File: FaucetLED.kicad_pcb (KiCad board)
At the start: 2 copper layers, 29.2 x 33.3 mm, 25 parts, among them P1 CONN_01X13, P2 CONN_01X02, U1 MAX4256

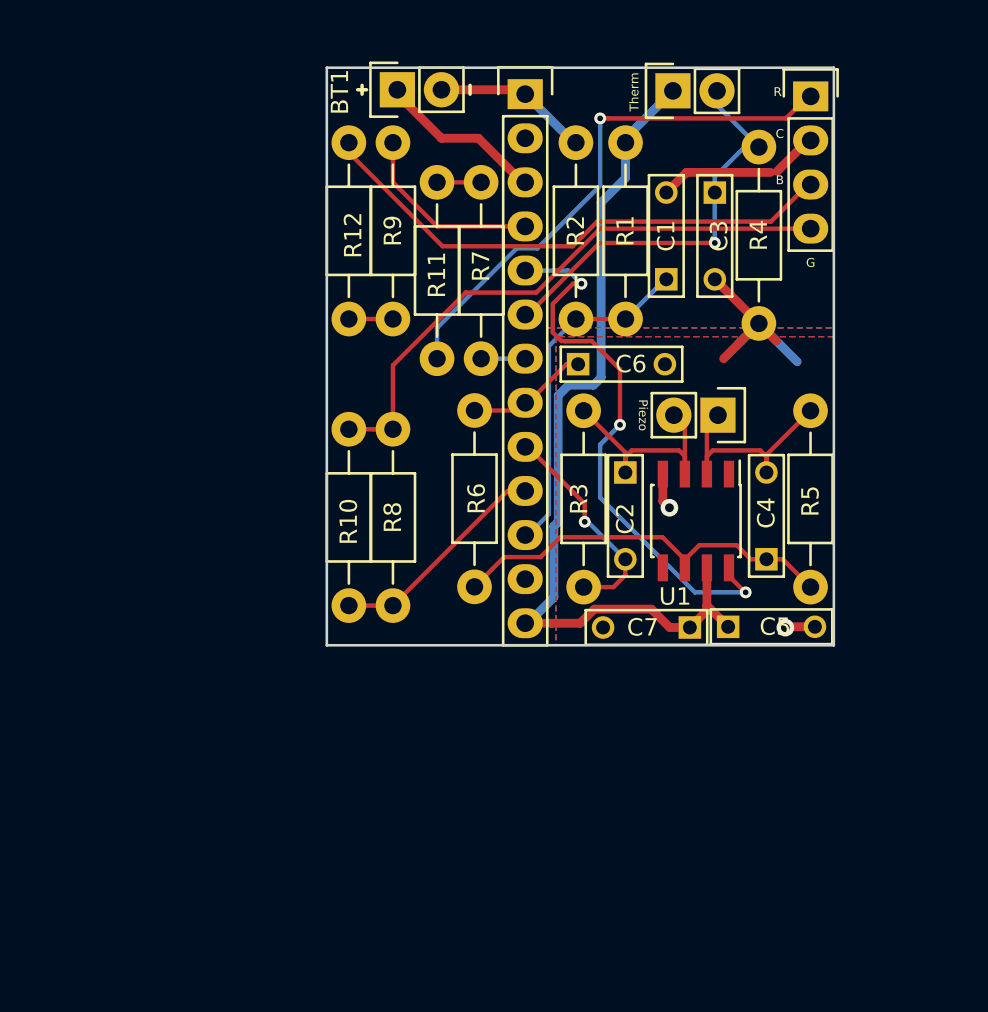
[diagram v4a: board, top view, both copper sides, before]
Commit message: WIP version 2 with STM32L0.
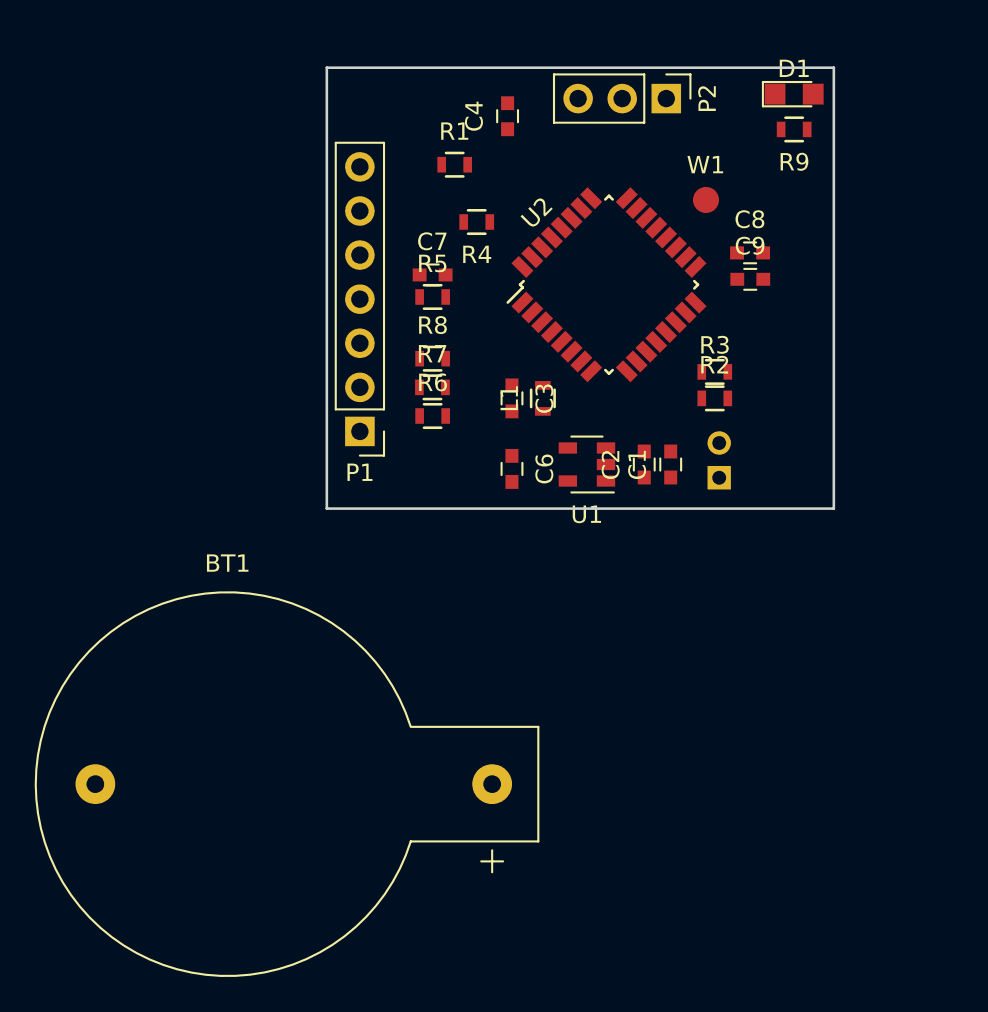
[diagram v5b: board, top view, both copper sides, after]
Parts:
- removed C5: 0.1u, Capacitors_ThroughHole:C_Rect_L7_W2_P5
- removed R10: 68R, Resistors_ThroughHole:Resistor_Horizontal_RM10mm
- removed R11, R12: 10R, Resistors_ThroughHole:Resistor_Horizontal_RM10mm
- removed TH1: THERMISTOR, Pin_Headers:Pin_Header_Straight_1x02
- added BT2: LiIon, Pin_Headers:Pin_Header_Angled_1x02_Pitch2.00mm, B.Cu at (124.2, 99.8)
- added C8: 0.1u, Capacitors_SMD:C_0603, F.Cu at (126.0, 86.9)
- added C9: 1u, Capacitors_SMD:C_0603, F.Cu at (126.0, 88.4)
- added L1: Bead, Resistors_SMD:R_0603, F.Cu at (114.0, 95.2)
- added U2: STM32L052KxTx, Housings_QFP:LQFP-32_7x7mm_Pitch0.8mm, F.Cu at (117.9, 88.7)
- added W1: TEST_1P, Measurement_Points:Measurement_Point_Round-SMD-Pad_Small, F.Cu at (123.4, 83.8)
- BT1: value Battery -> CR2016x2; footprint Pin_Headers:Pin_Header_Straight_1x02 -> Connect:CR2032H
- C1: value 10n -> 0.1u; footprint Capacitors_ThroughHole:C_Rect_L7_W2_P5 -> Capacitors_SMD:C_0603
- C2: value 10p -> 1u; footprint Capacitors_ThroughHole:C_Rect_L7_W2_P5 -> Capacitors_SMD:C_0603
- C3, C7: value 1u -> 0.1u; footprint Capacitors_ThroughHole:C_Rect_L7_W2_P5 -> Capacitors_SMD:C_0603
- C4: value 10p -> 0.47u; footprint Capacitors_ThroughHole:C_Rect_L7_W2_P5 -> Capacitors_SMD:C_0603
- C6: value 0.1u -> 1u; footprint Capacitors_ThroughHole:C_Rect_L7_W2_P5 -> Capacitors_SMD:C_0603
- D1: value LED_RCBG -> LED; footprint Pin_Headers:Pin_Header_Straight_1x04 -> LEDs:LED_0805
- P1: value CONN_01X13 -> CONN_01X07; footprint Socket_Strips:Socket_Strip_Straight_1x13 -> Pin_Headers:Pin_Header_Straight_1x07_Pitch2.54mm
- P2: value CONN_01X02 -> CONN_01X03; footprint Pin_Headers:Pin_Header_Straight_1x02 -> Pin_Headers:Pin_Header_Straight_1x03_Pitch2.54mm
- R1: value 1M -> 100R; footprint Resistors_ThroughHole:Resistor_Horizontal_RM10mm -> Resistors_SMD:R_0603
- R2, R4: footprint Resistors_ThroughHole:Resistor_Horizontal_RM10mm -> Resistors_SMD:R_0603
- R3: value 100M -> 1M; footprint Resistors_ThroughHole:Resistor_Horizontal_RM10mm -> Resistors_SMD:R_0603
- R5: value 100M -> 10k; footprint Resistors_ThroughHole:Resistor_Horizontal_RM10mm -> Resistors_SMD:R_0603
- R6: value 680R -> 78R; footprint Resistors_ThroughHole:Resistor_Horizontal_RM10mm -> Resistors_SMD:R_0603
- R7: value 68R -> 12R; footprint Resistors_ThroughHole:Resistor_Horizontal_RM10mm -> Resistors_SMD:R_0603
- R8: value 15R -> 25R; footprint Resistors_ThroughHole:Resistor_Horizontal_RM10mm -> Resistors_SMD:R_0603
- R9: value 15R -> 1k; footprint Resistors_ThroughHole:Resistor_Horizontal_RM10mm -> Resistors_SMD:R_0603
- U1: value MAX4256 -> TLV70033DDC; footprint Housings_SOIC:SOIC-8_3.9x4.9mm_Pitch1.27mm -> TO_SOT_Packages_SMD:SOT-23-5
- moved BT1 40.4 mm to (111.1, 117.5), turned to 0 degrees
- moved C4 29.6 mm to (112.0, 79.0)
- moved R5 27.4 mm to (107.7, 89.4), turned to 0 degrees
- moved R9 25.6 mm to (128.5, 79.8), turned to 180 degrees
- moved C7 25.1 mm to (107.7, 88.1), turned to 0 degrees
- moved P1 21.6 mm to (103.5, 97.2), turned to 180 degrees
- moved P2 18.5 mm to (121.2, 78.0)
- moved R4 16.8 mm to (110.2, 85.1), turned to 180 degrees
- moved C3 16.6 mm to (112.3, 95.2)
- moved R7 12.1 mm to (107.7, 94.6), turned to 0 degrees
- moved C1 10.7 mm to (121.4, 99.1)
- moved R1 9.92 mm to (109.0, 81.8), turned to 0 degrees
- moved R2 9.22 mm to (124.0, 95.2), turned to 0 degrees
- moved R3 7.88 mm to (124.0, 93.7), turned to 0 degrees
- moved C6 7.13 mm to (112.3, 99.3), turned to 270 degrees
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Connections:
- C1 pad 1: /VCC_2 -> +BATT
- C2 pad 1: /PIEZO_2 -> +BATT
- C2 pad 2: /VCC_2_BUF -> GND
- C3 pad 1: /THERM_2 -> /RESET
- C4 pad 1: Net-(C4-Pad1) -> /TSC_SAMPLING
- C4 pad 2: /PIEZO_1 -> GND
- C6 pad 1: /PIEZO_AMP -> +3V3
- C7 pad 1: +3V3 -> /THERM_SENSE
- D1 pad 1: Net-(D1-Pad1) -> GND
- D1 pad 2: GND -> Net-(D1-Pad2)
- P1 pad 1: GND -> /LED_R_OUT
- P1 pad 2: (no net) -> /LED_G_OUT
- P1 pad 3: +BATT -> /LED_B_OUT
- P1 pad 4: /LED_B -> GND
- P1 pad 5: /AMP_SHDN -> /THERM_SW
- P1 pad 6: /THERM_2 -> /THERM_SENSE
- P1 pad 7: /LED_R -> /TSC_IN
- P2 pad 1: /PIEZO_1 -> /SWDIO
- P2 pad 2: /PIEZO_2 -> /SWCLK
- R1 pad 1: +3V3 -> /TSC_IN
- R1 pad 2: /VCC_2 -> Net-(R1-Pad2)
- R2 pad 1: /VCC_2 -> +BATT
- R2 pad 2: GND -> /BATT_2
- R3 pad 1: /PIEZO_2 -> /BATT_2
- R3 pad 2: /VCC_2_BUF -> GND
- R4 pad 1: /THERM_2 -> Net-(R4-Pad1)
- R5 pad 1: Net-(C4-Pad1) -> /THERM_SW
- R5 pad 2: /PIEZO_1 -> /THERM_SENSE
- R6 pad 1: /PIEZO_AMP -> /LED_R_OUT
- R6 pad 2: Net-(C4-Pad1) -> /LED_R
- R7 pad 1: Net-(R11-Pad2) -> /LED_G_OUT
- R7 pad 2: /LED_R -> /LED_G
- R8 pad 1: Net-(D1-Pad4) -> /LED_B_OUT
- R8 pad 2: /LED_G -> /LED_B
- R9 pad 1: Net-(R12-Pad2) -> Net-(D1-Pad2)
- R9 pad 2: /LED_B -> /LED_DBG
- U1 pad 1: (no net) -> +BATT
- U1 pad 2: /PIEZO_1 -> GND
- U1 pad 3: /PIEZO_2 -> +BATT
- U1 pad 4: GND -> (no net)
- U1 pad 5: (no net) -> +3V3
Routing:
- net +3V3: track 51.4 -> 0.00 mm
- net GND: track 35.2 -> 0.00 mm, vias 2 -> 0
- net Net-(D1-Pad4): track 33.6 -> 0.00 mm
- net /AMP_SHDN: track 32.6 -> 0.00 mm, vias 3 -> 0
- net Net-(D1-Pad1): track 31.1 -> 0.00 mm, vias 1 -> 0
- net Net-(D1-Pad3): track 30.9 -> 0.00 mm
- net /THERM_2: track 25.5 -> 0.00 mm, vias 1 -> 0
- net Net-(C4-Pad1): track 23.4 -> 0.00 mm
- net /VCC_2: track 20.2 -> 0.00 mm
- net /VCC_2_BUF: track 14.4 -> 0.00 mm, vias 1 -> 0
- net /PIEZO_1: track 13.9 -> 0.00 mm
- net /PIEZO_2: track 13.9 -> 0.00 mm
- net /LED_G: track 13.6 -> 0.00 mm
- net /LED_B: track 10.5 -> 0.00 mm
- net +BATT: track 9.72 -> 0.00 mm
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- removed copper zone on B.Cu, net GND
- removed copper zone on F.Cu, net GND
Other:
- board size 29.2 x 33.3 mm -> 29.2 x 25.4 mm
- board text removed: "B"
- board text removed: "C"
- board text removed: "FaucetLED v1.0 Nick Graumann"
- board text removed: "G"
- board text removed: "Piezo"
- board text removed: "R"
- board text removed: "Therm"

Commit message: Add battery holder, more connectors.
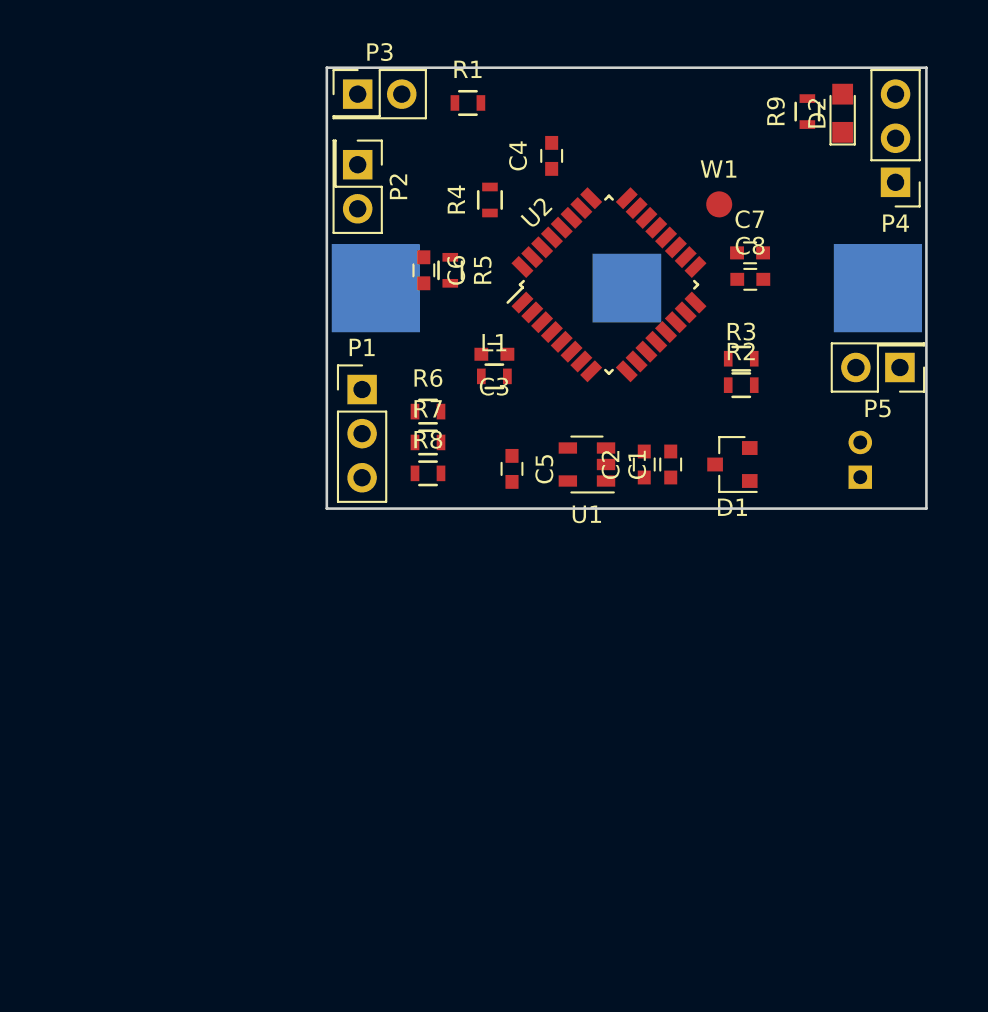
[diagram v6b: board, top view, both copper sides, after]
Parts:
- added D1: D_Schottky_x2_KCom_AAK, TO_SOT_Packages_SMD:SOT-23, F.Cu at (125.0, 99.1)
- added P2: CONN_01X02, Pin_Headers:Pin_Header_Straight_2x01_Pitch2.54mm, F.Cu at (103.4, 81.8)
- added P3: CONN_01X02, Pin_Headers:Pin_Header_Straight_2x01_Pitch2.54mm, F.Cu at (103.4, 77.7)
- added P5: CONN_01X02, Pin_Headers:Pin_Header_Straight_2x01_Pitch2.54mm, F.Cu at (134.6, 93.5)
- BT1: footprint Connect:CR2032H -> components:Keystone_3020_CR2016x2; moved to B.Cu
- P1: value CONN_01X07 -> CONN_01X03; footprint Pin_Headers:Pin_Header_Straight_1x07_Pitch2.54mm -> Pin_Headers:Pin_Header_Straight_1x03_Pitch2.54mm
- moved BT1 29.6 mm to (118.9, 88.9), turned to 180 degrees
- moved P4 14.1 mm to (134.4, 82.8), turned to 180 degrees
- moved BT2 8.13 mm to (132.3, 99.8)
- moved R8 6.61 mm to (107.4, 99.6)
- moved R1 3.64 mm to (109.7, 78.2)
- moved C4 3.42 mm to (114.6, 81.3)
- moved R7 3.19 mm to (107.4, 97.8)
- moved L1 3.07 mm to (111.3, 94.0), turned to 0 degrees
- moved D2 3.00 mm to (131.3, 78.8), turned to 90 degrees
- moved C3 2.74 mm to (111.3, 92.7), turned to 180 degrees
- moved P1 2.42 mm to (103.6, 94.7), turned to 0 degrees
- moved R5 1.84 mm to (108.7, 87.9), turned to 270 degrees
- moved R2 1.70 mm to (125.5, 94.5)
- moved R3 1.70 mm to (125.5, 93.0)
- moved R4 1.48 mm to (111.0, 83.8), turned to 90 degrees
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- renumbered C6 to C5, C7 to C6, C8 to C7, C9 to C8, D1 to D2, P2 to P4
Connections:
- BT1 pad 1: +BATT -> Net-(BT1-Pad1)
- BT2 pad 1: +BATT -> Net-(BT2-Pad1)
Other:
- board size 29.2 x 25.4 mm -> 34.5 x 25.4 mm

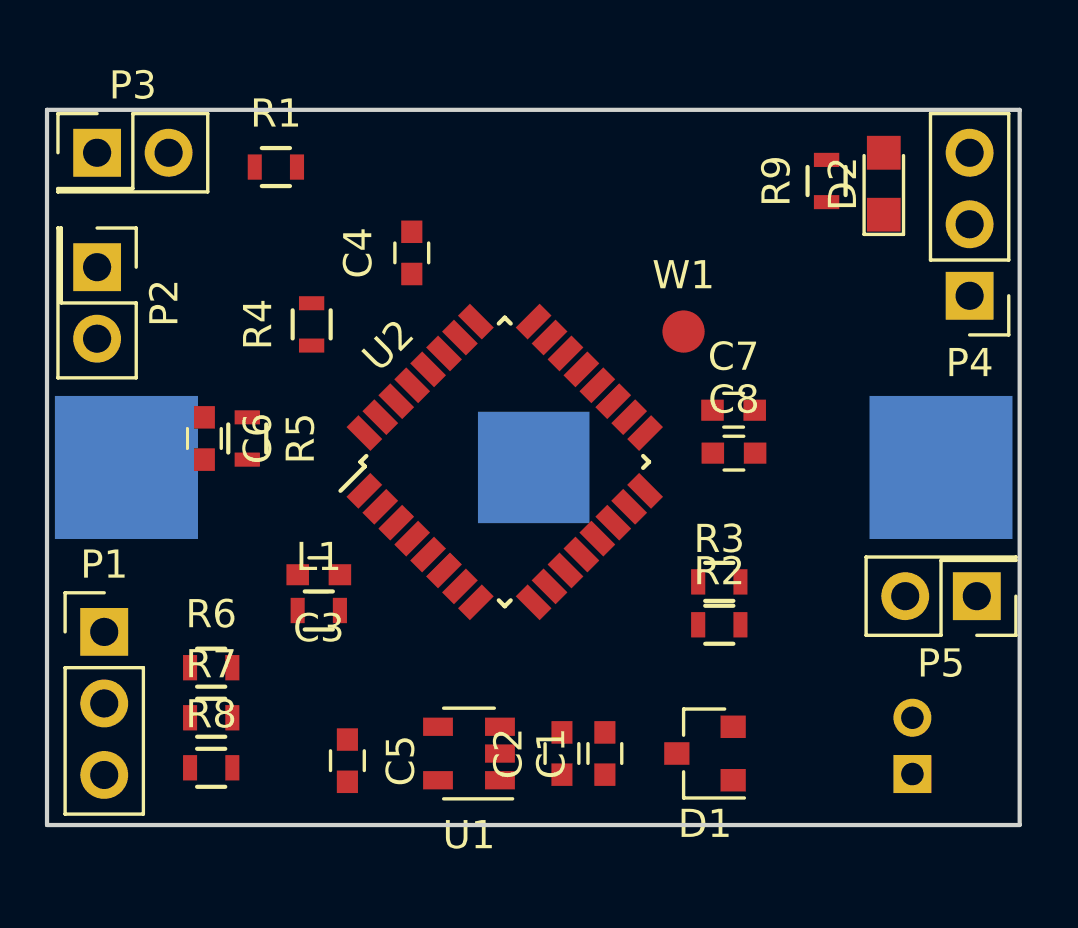
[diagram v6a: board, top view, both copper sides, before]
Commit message: Update R and C footprints for 0603/0805 compatibility.
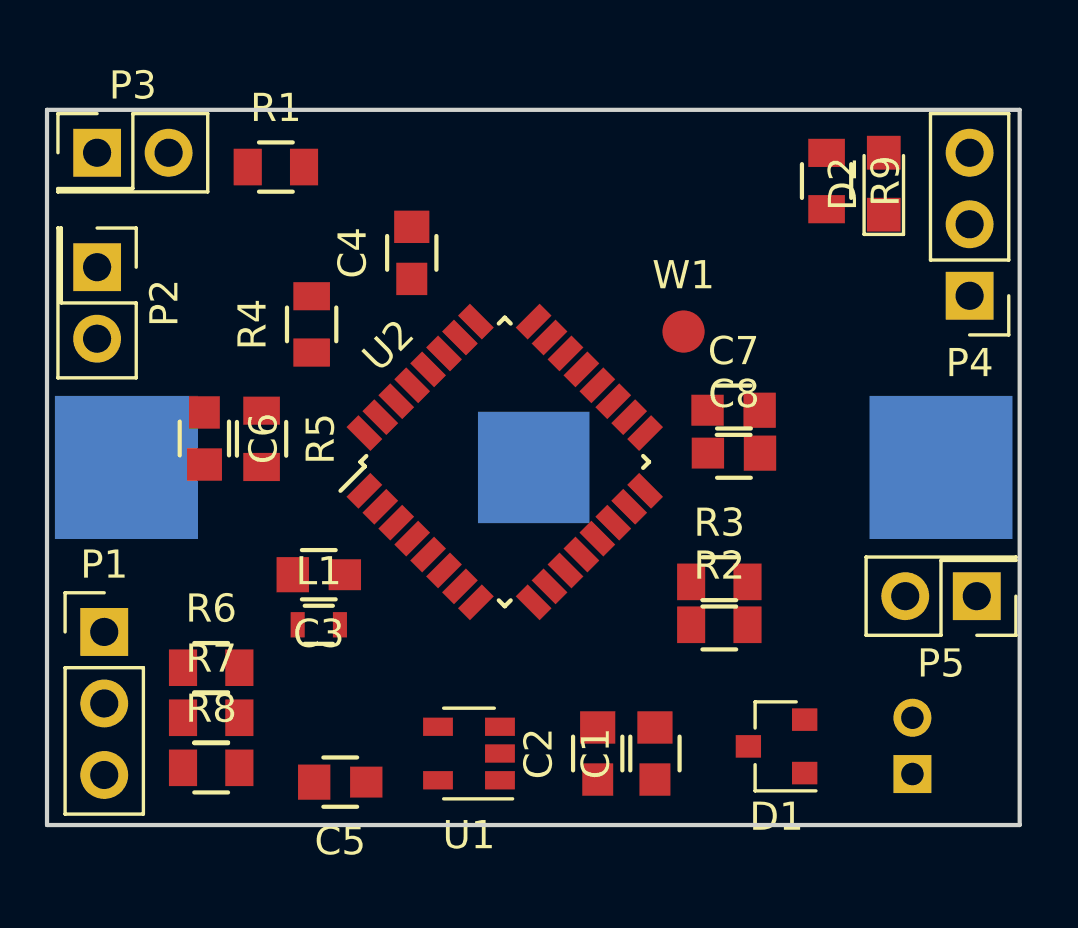
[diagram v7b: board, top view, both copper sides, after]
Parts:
- C1, C2, C3, C4, C5, C6, C7, C8: footprint Capacitors_SMD:C_0603 -> components:C_0603_0805
- R1, R2, R3, R4, R5, R6, R7, R8, R9: footprint Resistors_SMD:R_0603 -> components:R_0603_0805
- moved D1 2.55 mm to (127.5, 98.8)
- moved C1 1.78 mm to (123.2, 99.1)
- moved C2 1.27 mm to (121.2, 99.1)
- moved C5 0.80 mm to (112.0, 100.1), turned to 180 degrees
- moved R5 0.51 mm to (109.2, 87.9)
- moved L1 0.51 mm to (111.3, 94.5)
